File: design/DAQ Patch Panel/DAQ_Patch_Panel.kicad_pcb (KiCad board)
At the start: 2 copper layers, 43.8 x 129.3 mm, 43 parts, among them J1 Power Terminal 1, J2 Data Output Terminal, J3 Power Terminal 2, J4 Weidmuller LM3RZF

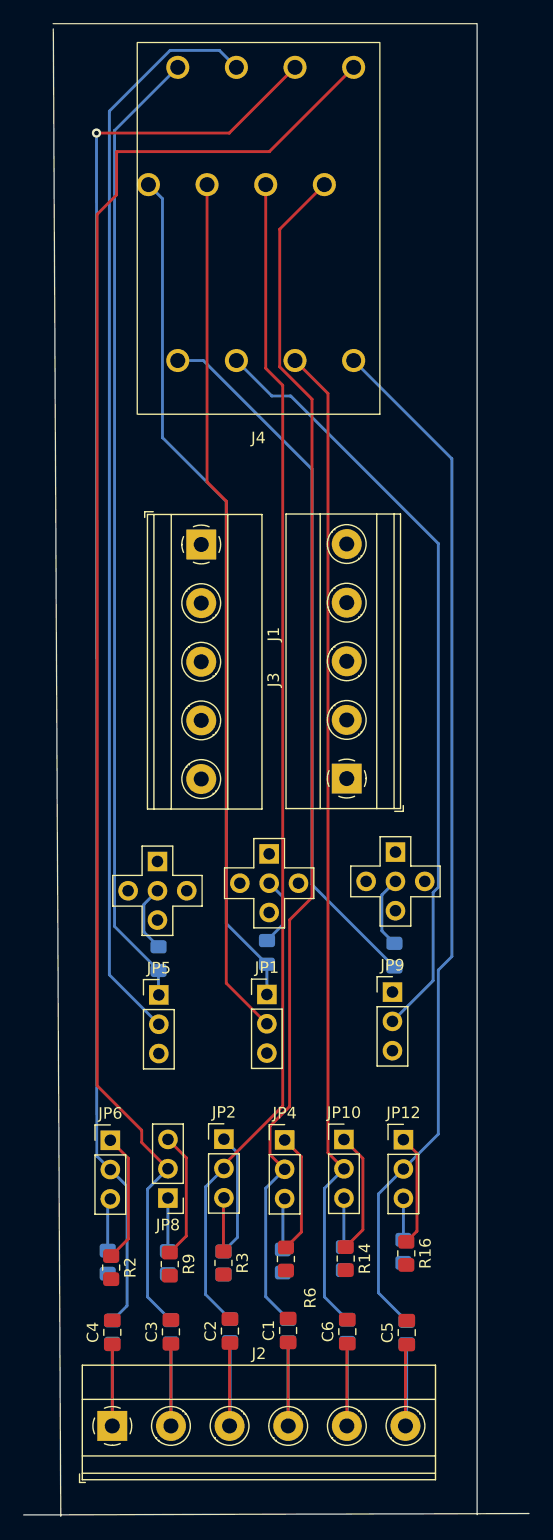
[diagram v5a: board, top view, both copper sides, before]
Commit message: Routing Changes, Pours Added
Needs to be tidied up before review
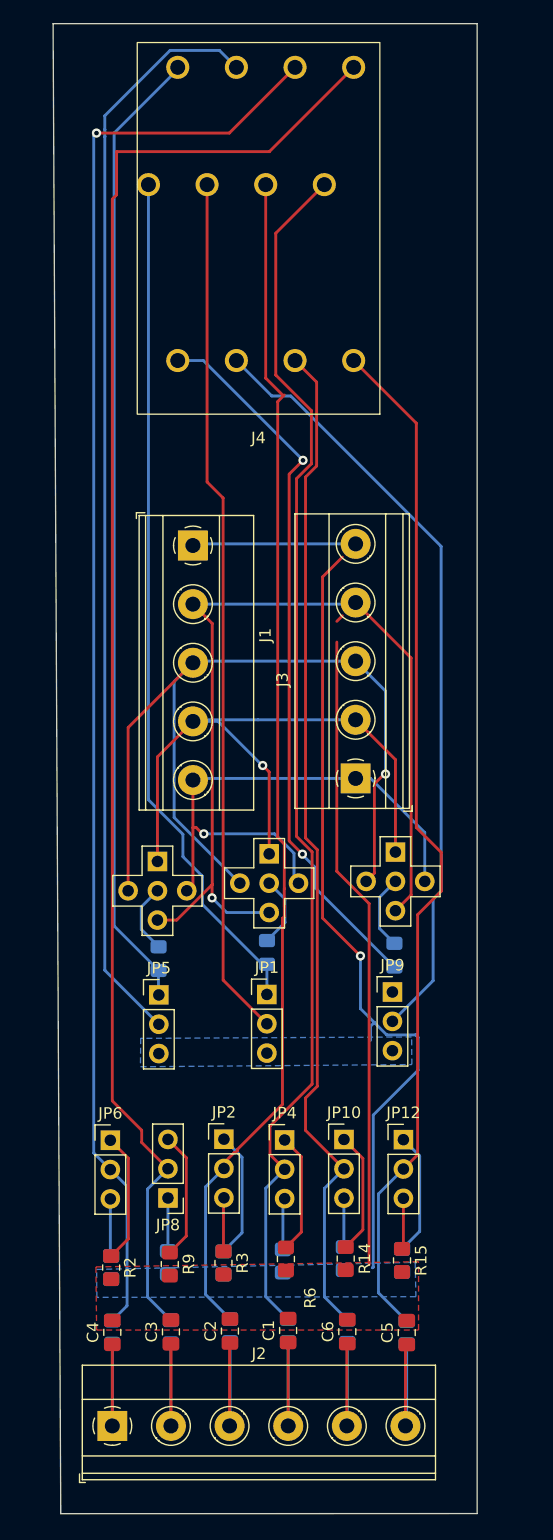
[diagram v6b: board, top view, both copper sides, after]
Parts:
- R15: moved to F.Cu
- R16: moved to B.Cu
- moved R15 0.80 mm to (149.0, 153.4)
- moved J3 0.77 mm to (144.9, 111.6)
- moved J1 0.73 mm to (130.8, 91.5)
- moved R16 0.71 mm to (149.0, 153.4)
- moved R1 0.56 mm to (123.8, 154.0)
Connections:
- J1 pad 1: +20V -> GND
- J1 pad 2: +12V -> +5V
- J1 pad 4: +5V -> +12V
- J1 pad 5: GND -> +20V
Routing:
- net (no net): track 0.00 -> 126.4 mm, vias 0 -> 1
- net +5V: track 0.00 -> 80.9 mm, vias 0 -> 1
- net +10V: track 0.00 -> 79.5 mm, vias 0 -> 1
- net +12V: track 0.00 -> 56.0 mm, vias 0 -> 1
- net +20V: track 0.00 -> 48.8 mm, vias 0 -> 1
- net GND: track 0.00 -> 14.2 mm
- net /S3IN1: track 86.4 -> 88.0 mm
- net /S2IN2: track 104.6 -> 105.9 mm
- net /S3POWER: track 61.6 -> 62.8 mm, vias 0 -> 2
- net /S1IN2: track 129.6 -> 128.5 mm
- net /S2IN1: track 102.5 -> 103.5 mm
- net Net-(JP12-A): track 9.72 -> 10.7 mm
- net Net-(JP12-B): track 3.59 -> 4.43 mm
- net /S3IN2: track 90.4 -> 89.6 mm
- net Net-(JP6-B): track 4.58 -> 5.31 mm
- added copper zone on B.Cu, net (none)
- added copper zone on F.Cu, net (none)
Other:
- board size 43.8 x 129.3 mm -> 36.7 x 129.1 mm

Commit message: Something
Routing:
- net (no net): track 126.4 -> 72.0 mm
- net +12V: track 56.0 -> 51.7 mm
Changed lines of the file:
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@@
   (gr_line (start 119.395 175.33) (end 155.47 175.32)
     (stroke (width 0.1) (type default)) (layer "Edge.Cuts"))
+  (segment (start 146.18 127.83) (end 145.36 127.01) (width 0.25) (layer "F.Cu") (net 0))
   (segment (start 142.0746 123.7246) (end 142.0746 94.1754) (width 0.25) (layer "F.Cu") (net 0))
-  (segment (start 143.3118 98.0182) (end 143.792186 97.537814) (width 0.25) (layer "F.Cu") (net 0))
-  (segment (start 146.11 122.47458) (end 143.3118 119.67638) (width 0.25) (layer "F.Cu") (net 0))
   (segment (start 142.0746 94.1754) (end 143.792186 92.457814) (width 0.25) (layer "F.Cu") (net 0))
-  (segment (start 146.11 153.75) (end 146.11 122.47458) (width 0.25) (layer "F.Cu") (net 0))
-  (segment (start 143.3118 119.67638) (end 143.3118 99.82) (width 0.25) (layer "F.Cu") (net 0))
+  (segment (start 146.18 153.94) (end 146.18 127.83) (width 0.25) (layer "F.Cu") (net 0))
   (segment (start 145.36 127.01) (end 142.0746 123.7246) (width 0.25) (layer "F.Cu") (net 0))
   (via (at 145.36 127.01) (size 0.8) (drill 0.4) (layers "F.Cu" "B.Cu") (net 0))
-  (segment (start 150.178956 133.851044) (end 150.14 133.851044) (width 0.25) (layer "B.Cu") (net 0))
-  (segment (start 146.4668 140.7932) (end 150.35 136.91) (width 0.25) (layer "B.Cu") (net 0))
-  (segment (start 146.4 154.02) (end 146.42 154.02) (width 0.25) (layer "B.Cu") (net 0))
   (segment (start 145.36 131.57208) (end 145.36 127.01) (width 0.25) (layer "B.Cu") (net 0))
-  (segment (start 147.638964 133.851044) (end 146.55896 132.77104) (width 0.25) (layer "B.Cu") (net 0))
-  (segment (start 150.35 134.061044) (end 150.14 133.851044) (width 0.25) (layer "B.Cu") (net 0))
-  (segment (start 150.35 136.91) (end 150.35 134.061044) (width 0.25) (layer "B.Cu") (net 0))
   (segment (start 146.23 133.1) (end 146.55896 132.77104) (width 0.25) (layer "B.Cu") (net 0))
-  (segment (start 146.4668 153.9732) (end 146.4668 140.7932) (width 0.25) (layer "B.Cu") (net 0))
   (segment (start 145.4 126.97) (end 145.35 126.92) (width 0.25) (layer "B.Cu") (net 0))
   (segment (start 146.55896 132.77104) (end 145.36 131.57208) (width 0.25) (layer "B.Cu") (net 0))
-  (segment (start 146.42 154.02) (end 146.4668 153.9732) (width 0.25) (layer "B.Cu") (net 0))
   (segment (start 145.36 127.01) (end 145.4 126.97) (width 0.25) (layer "B.Cu") (net 0))
-  (segment (start 150.14 133.851044) (end 147.638964 133.851044) (width 0.25) (layer "B.Cu") (net 0))
   (segment (start 146.23 134.32) (end 146.23 133.1) (width 0.25) (layer "B.Cu") (net 0))
   (segment (start 139.1 160.5075) (end 139.09 160.4975) (width 0.25) (layer "F.Cu") (net 1))
@@
   (segment (start 137.45 111.07) (end 137.45 118.1675) (width 0.25) (layer "F.Cu") (net 15))
   (via (at 136.89 110.51) (size 0.8) (drill 0.4) (layers "F.Cu" "B.Cu") (net 15))
-  (segment (start 144.94 106.55) (end 136.48 106.55) (width 0.25) (layer "B.Cu") (net 15))
-  (segment (start 136.48 106.55) (end 130.985 106.55) (width 0.25) (layer "B.Cu") (net 15))
+  (segment (start 140.85 106.55) (end 144.94 106.55) (width 0.25) (layer "B.Cu") (net 15))
+  (segment (start 136.89 110.51) (end 140.85 106.55) (width 0.25) (layer "B.Cu") (net 15))
   (segment (start 136.85 110.51) (end 136.89 110.51) (width 0.25) (layer "B.Cu") (net 15))
   (segment (start 136.89 110.55) (end 136.89 110.55) (width 0.25) (layer "B.Cu") (net 15))
@@
     (connect_pads (clearance 0.5))
     (min_thickness 0.25) (filled_areas_thickness no)
-    (fill (thermal_gap 0.5) (thermal_bridge_width 0.5) (island_removal_mode 1) (island_area_min 10))
+    (fill yes (thermal_gap 0.5) (thermal_bridge_width 0.5) (island_removal_mode 1) (island_area_min 10))
     (polygon
       (pts
@@
       )
     )
-  )
-  (zone (net 0) (net_name "") (layer "B.Cu") (hatch edge 0.5)
-    (priority 1)
-    (connect_pads (clearance 0.5))
-    (min_thickness 0.25) (filled_areas_thickness no)
-    (fill yes (thermal_gap 0.5) (thermal_bridge_width 0.5) (island_removal_mode 1) (island_area_min 10))
-    (polygon
-      (pts
-        (xy 122.5 154.17)
-        (xy 150.1 153.55)
-        (xy 150.16 156.53)
-        (xy 122.52 156.59)
-      )
-    )

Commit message: Tried to Pour
Tryed to pour,
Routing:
- net (no net): track 72.0 -> 43.5 mm
- net GND: track 14.2 -> 20.9 mm
- added copper zone on F.Cu, net GND
- removed copper zone on F.Cu, net (none)
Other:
- board size 36.7 x 129.1 mm -> 33 x 129.1 mm
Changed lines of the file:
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@@
     )
   )
-  (gr_line (start 155.465 46.24) (end 118.73 46.24)
+  (gr_line (start 153.31375 46.26) (end 120.38 46.26)
     (stroke (width 0.1) (type default)) (layer "Edge.Cuts"))
-  (gr_line (start 155.47 175.32) (end 155.465 46.24)
+  (gr_line (start 153.31375 175.33) (end 153.31375 46.26)
     (stroke (width 0.1) (type default)) (layer "Edge.Cuts"))
-  (gr_line (start 118.73 46.24) (end 119.395 175.33)
+  (gr_line (start 120.38 46.26) (end 120.38 175.28)
     (stroke (width 0.1) (type default)) (layer "Edge.Cuts"))
-  (gr_line (start 119.395 175.33) (end 155.47 175.32)
+  (gr_line (start 120.38 175.28) (end 153.33 175.33)
     (stroke (width 0.1) (type default)) (layer "Edge.Cuts"))
-  (segment (start 146.18 127.83) (end 145.36 127.01) (width 0.25) (layer "F.Cu") (net 0))
+  (dimension (type orthogonal) (layer "F.Cu")
+    (pts (xy 119.12 46.24) (xy 155.465 46.24))
+    (height -2.97)
+    (orientation 0)
+    (gr_text "36.3450 mm" (at 137.2925 41.47) (layer "F.Cu")
+      (effects (font (size 1.5 1.5) (thickness 0.3)))
+    )
+    (format (prefix "") (suffix "") (units 3) (units_format 1) (precision 4))
+    (style (thickness 0.2) (arrow_length 1.27) (text_position_mode 0) (extension_height 0.58642) (extension_offset 0.5) keep_text_aligned)
+  )
+  (dimension (type orthogonal) (layer "F.Cu")
+    (pts (xy 155.465 46.24) (xy 155.5175 175.335))
+    (height 13.655)
+    (orientation 1)
+    (gr_text "129.0950 mm" (at 167.32 110.7875 90) (layer "F.Cu")
+      (effects (font (size 1.5 1.5) (thickness 0.3)))
+    )
+    (format (prefix "") (suffix "") (units 3) (units_format 1) (precision 4))
+    (style (thickness 0.2) (arrow_length 1.27) (text_position_mode 0) (extension_height 0.58642) (extension_offset 0.5) keep_text_aligned)
+  )
   (segment (start 142.0746 123.7246) (end 142.0746 94.1754) (width 0.25) (layer "F.Cu") (net 0))
   (segment (start 142.0746 94.1754) (end 143.792186 92.457814) (width 0.25) (layer "F.Cu") (net 0))
-  (segment (start 146.18 153.94) (end 146.18 127.83) (width 0.25) (layer "F.Cu") (net 0))
   (segment (start 145.36 127.01) (end 142.0746 123.7246) (width 0.25) (layer "F.Cu") (net 0))
   (via (at 145.36 127.01) (size 0.8) (drill 0.4) (layers "F.Cu" "B.Cu") (net 0))
@@
   (segment (start 146.55896 132.77104) (end 145.36 131.57208) (width 0.25) (layer "B.Cu") (net 0))
   (segment (start 145.36 127.01) (end 145.4 126.97) (width 0.25) (layer "B.Cu") (net 0))
-  (segment (start 146.23 134.32) (end 146.23 133.1) (width 0.25) (layer "B.Cu") (net 0))
   (segment (start 139.1 160.5075) (end 139.09 160.4975) (width 0.25) (layer "F.Cu") (net 1))
   (segment (start 139.1 167.7275) (end 139.1 160.5075) (width 0.25) (layer "F.Cu") (net 1))
   (segment (start 139.09 160.4675) (end 139.09 167.7175) (width 0.25) (layer "B.Cu") (net 1))
   (segment (start 139.09 167.7175) (end 139.1 167.7275) (width 0.25) (layer "B.Cu") (net 1))
+  (segment (start 133.49 154.6075) (end 133.48 156.32) (width 0.25) (layer "B.Cu") (net 2))
+  (segment (start 128.68 154.5675) (end 128.68 156.22) (width 0.25) (layer "B.Cu") (net 2))
+  (segment (start 138.64 154.4375) (end 138.64 156.01) (width 0.25) (layer "B.Cu") (net 2))
   (segment (start 144.94 91.31) (end 130.985 91.31) (width 0.25) (layer "B.Cu") (net 2))
+  (segment (start 128.68 156.22) (end 128.7 156.24) (width 0.25) (layer "B.Cu") (net 2))
   (segment (start 130.985 91.31) (end 130.845 91.45) (width 0.25) (layer "B.Cu") (net 2))
+  (segment (start 123.81 156.71) (end 123.76 156.67) (width 0.25) (layer "B.Cu") (net 2))
+  (segment (start 133.48 156.32) (end 133.49 156.29) (width 0.25) (layer "B.Cu") (net 2))
+  (segment (start 123.76 155.01) (end 123.81 156.71) (width 0.25) (layer "B.Cu") (net 2))
   (segment (start 134.02 160.5775) (end 134.05 160.5475) (width 0.25) (layer "F.Cu") (net 3))
   (segment (start 134.02 167.7275) (end 134.02 160.5775) (width 0.25) (layer "F.Cu") (net 3))
@@
   (segment (start 149.08 152.27) (end 148.96 152.39) (width 0.25) (layer "F.Cu") (net 38))
   (segment (start 149.08 148.0075) (end 149.08 152.27) (width 0.25) (layer "F.Cu") (net 38))
-  (zone (net 0) (net_name "") (layer "F.Cu") (hatch edge 0.5)
+  (zone (net 2) (net_name "GND") (layer "F.Cu") (hatch edge 0.5)
     (priority 2)
     (connect_pads (clearance 0.5))
